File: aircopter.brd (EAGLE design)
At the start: 47 x 28 mm, 44 parts, among them IC1 STF202-22T1G, M1 WIRELESS-NRF24L01, U2 GY-521MPU6050, Y1 20 MHz

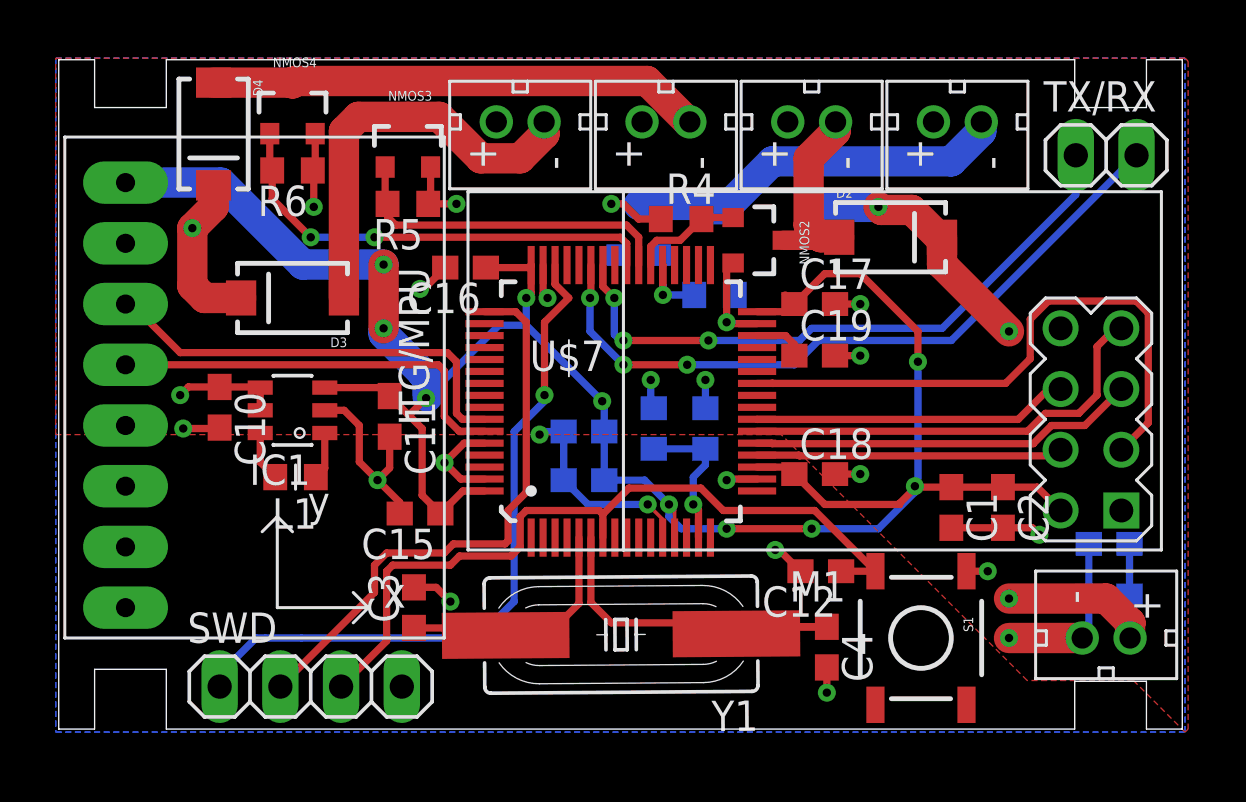
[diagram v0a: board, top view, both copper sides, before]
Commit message: Added Oshpark DRU, MGND and 3V3 planes
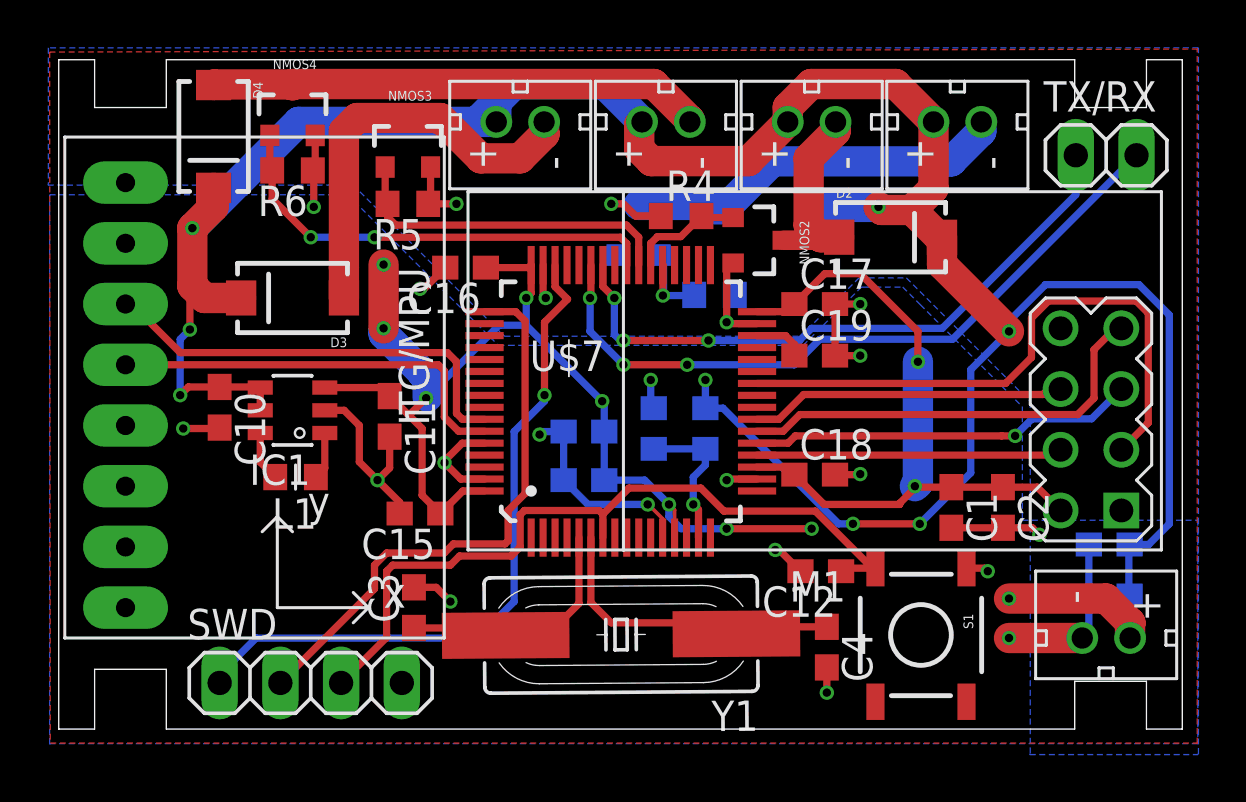
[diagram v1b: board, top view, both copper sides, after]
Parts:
- moved SWD 0.15 mm to (10.5, 1.93)
- moved R4 0.13 mm to (26.0, 21.5)
- moved S1 0.13 mm to (36.1, 3.94)
- moved D4 0.10 mm to (6.48, 24.8)
- moved NMOS4 0.08 mm to (9.78, 25.8)
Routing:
- net 3V7: track 33.0 -> 120.9 mm, vias 6 -> 9
- net 3V3: track 94.6 -> 76.5 mm
- net OSC0: track 5.37 -> 10.3 mm
- net GND: track 59.6 -> 61.7 mm
- net OSC1: track 11.9 -> 13.4 mm
- net SCK: vias 0 -> 1
- added copper zone on layer 1, net 3V3
- removed copper zone on layer 16, net 3V3
- removed copper zone on layer 1, net 3V7
